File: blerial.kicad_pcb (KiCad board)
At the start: 2 copper layers, 24 x 24 mm, 9 parts, among them J1 Header, SW1 Power Switch, U1 JDY-23-Module, U2 MIC5504-3.3YM5

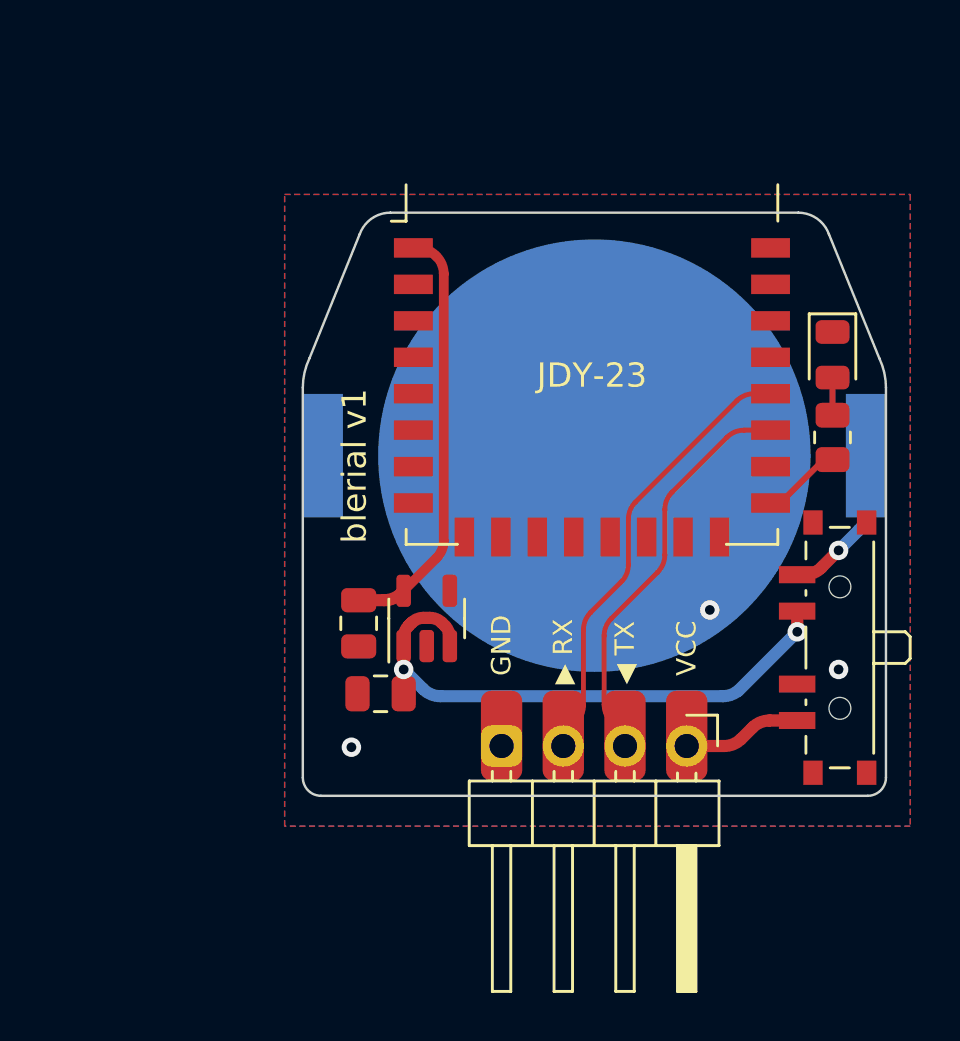
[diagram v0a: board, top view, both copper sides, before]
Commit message: edit to switch between bat / 3.3 regulator
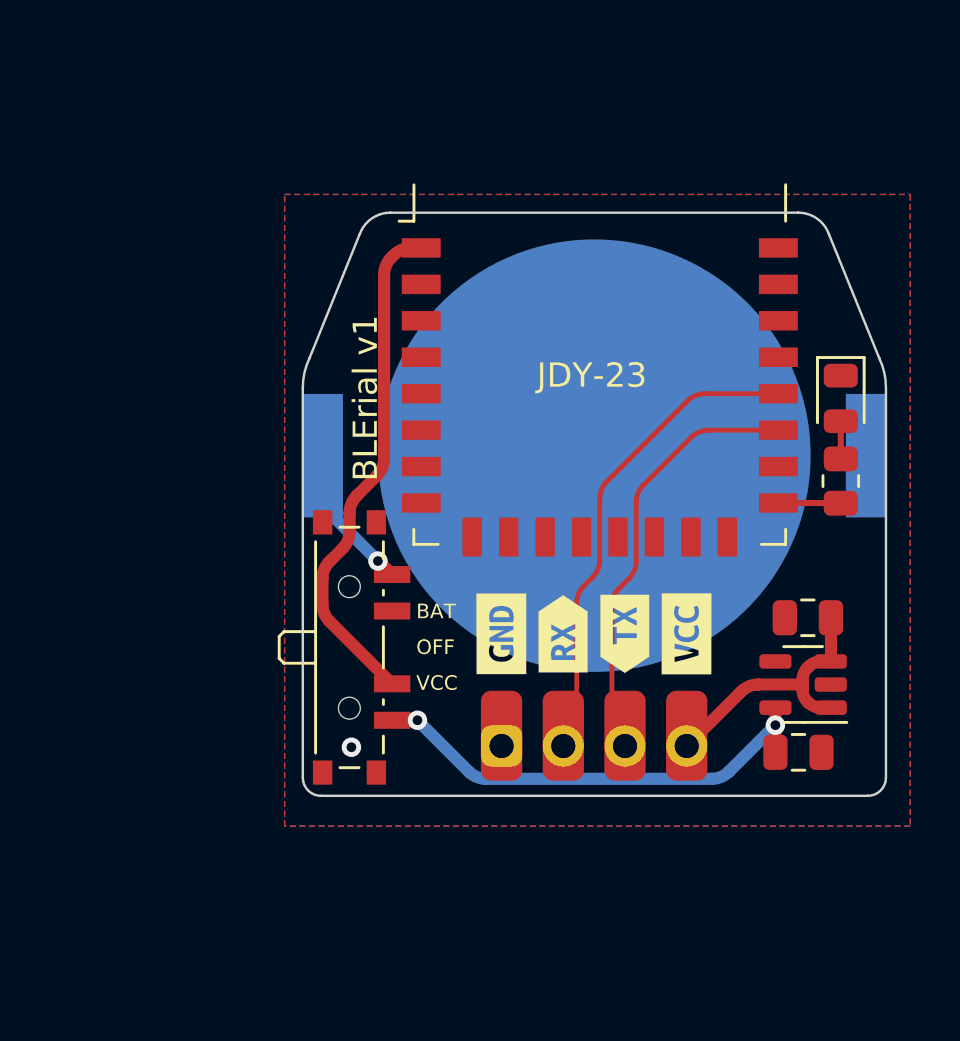
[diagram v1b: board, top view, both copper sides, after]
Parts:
- added kibuzzard-6213ECBD: G***, kibuzzard-6213ECBD, F.Cu at (159.2, 119.3)
- added kibuzzard-6213ECEC: G***, kibuzzard-6213ECEC, F.Cu at (161.7, 119.3)
- added kibuzzard-6213ECF8: G***, kibuzzard-6213ECF8, F.Cu at (164.3, 119.3)
- added kibuzzard-6213ED09: G***, kibuzzard-6213ED09, F.Cu at (166.8, 119.3)
- moved SW1 19.5 mm to (153.2, 119.9), turned to -90 degrees
- moved C2 18.9 mm to (171.4, 124.2), turned to 0 degrees
- moved C1 17.9 mm to (171.8, 118.7)
- moved U2 15.7 mm to (171.6, 121.4), turned to 180 degrees
- moved D1 1.83 mm to (173.1, 109.6)
- moved R1 1.83 mm to (173.1, 113.0)
- moved U1 0.32 mm to (163.2, 108.0)
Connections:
- BT1 pad 1: +BATT -> Net-(BT1-Pad1)
- C1 pad 1: Net-(U2-Pad1) -> VBUS
- J1 pad 1: VCC -> VBUS
- SW1 pad 1: VCC -> Net-(BT1-Pad1)
- SW1 pad 3: Net-(U2-Pad1) -> VCC
- SW1 pad 4: +BATT -> +3V3
- U1 pad 1: +3V3 -> VCC
- U2 pad 1: Net-(U2-Pad1) -> VBUS
- U2 pad 3: Net-(U2-Pad1) -> VBUS
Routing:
- net Net-(U2-Pad1): track 24.0 -> 0.00 mm, vias 2 -> 0
- net VCC: track 4.88 -> 21.0 mm
- net VBUS: track 0.00 -> 11.3 mm
- net +BATT: track 6.39 -> 0.00 mm, vias 1 -> 0
- net Net-(BT1-Pad1): track 0.00 -> 6.05 mm, vias 0 -> 1
- net +3V3: track 17.5 -> 19.4 mm, vias 0 -> 2
- net RXD: track 18.0 -> 19.5 mm
- net TXD: track 16.4 -> 17.3 mm
- net Net-(R1-Pad1): track 3.29 -> 2.56 mm
- net GND: vias 3 -> 1
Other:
- board text added: "2022 ansemjo"
- board text added: "BAT"
- board text added: "BLErial v1"
- board text added: "OFF"
- board text added: "VCC: 3.0-5.5V"
- board text removed: "GND"
- board text removed: "blerial v1"
- board text removed: "▶ RX"
- board text removed: "◀ TX"

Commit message: rerouted for HM-19, but not very tidy
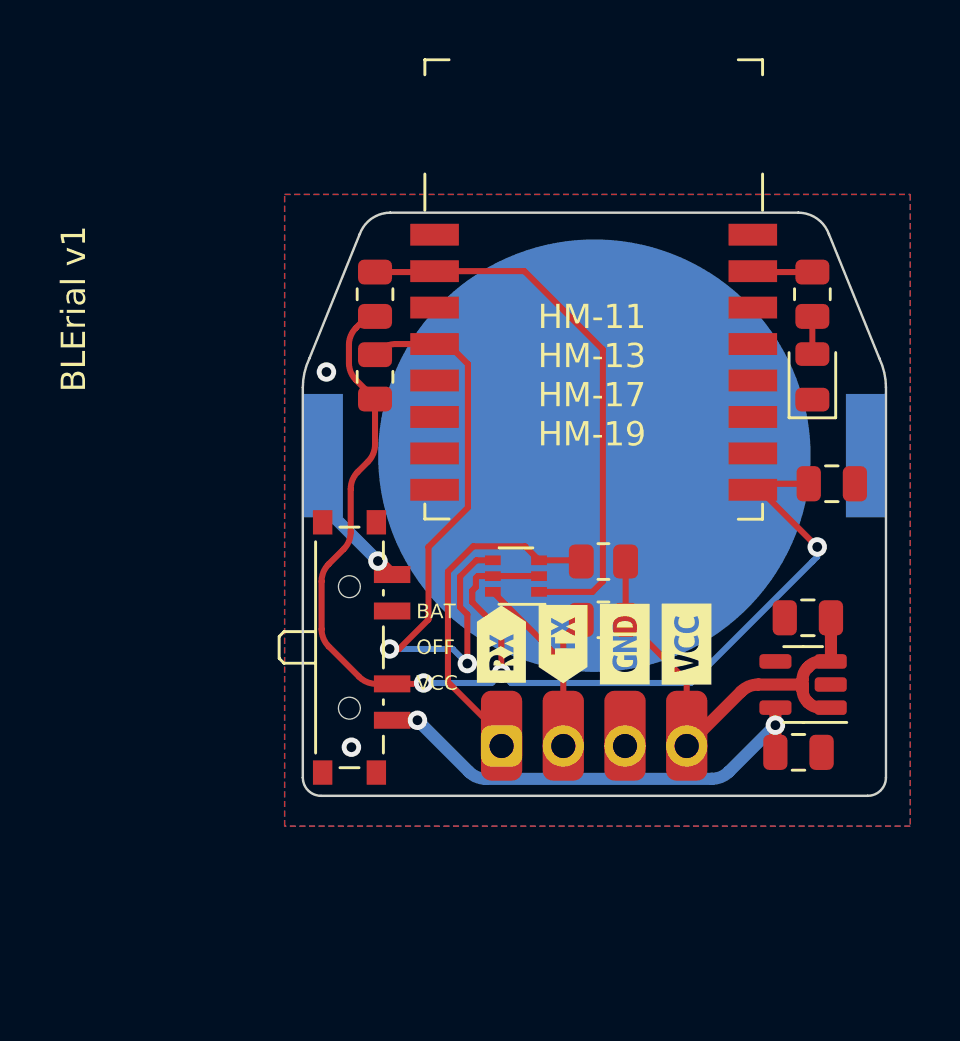
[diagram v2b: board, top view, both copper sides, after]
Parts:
- added C3: 0.1µF, Capacitor_SMD:C_0805_2012Metric, F.Cu at (172.8, 113.2)
- added Q1: BSD840N, Package_TO_SOT_SMD:SOT-363_SC-70-6, F.Cu at (159.8, 117.0)
- added R2: 10kΩ, Resistor_SMD:R_0805_2012Metric, F.Cu at (154.0, 105.4)
- added R3: 10kΩ, Resistor_SMD:R_0805_2012Metric, F.Cu at (163.4, 118.8)
- added R4: 10kΩ, Resistor_SMD:R_0805_2012Metric, F.Cu at (154.0, 108.8)
- added R5: 10kΩ, Resistor_SMD:R_0805_2012Metric, F.Cu at (163.4, 116.4)
- U1: value JDY-23-Module -> HM-19; footprint jdy:JDY-23 -> blerial:HM-19
- moved R1 7.78 mm to (172.0, 105.4)
- moved kibuzzard-6213ECBD 5.10 mm to (164.3, 119.8)
- moved kibuzzard-6213ECF8 2.57 mm to (161.7, 119.8)
- moved kibuzzard-6213ECEC 2.57 mm to (159.2, 119.8)
- moved D1 1.47 mm to (172.0, 108.8), turned to 90 degrees
- moved kibuzzard-6213ED09 0.42 mm to (166.8, 119.8)
- moved U1 0.25 mm to (163.0, 108.1)
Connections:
- J1 pad 2: TXD -> GND
- J1 pad 3: RXD -> TXD_H
- J1 pad 4: GND -> RXD_H
- R1 pad 1: Net-(R1-Pad1) -> Net-(D1-Pad2)
- R1 pad 2: Net-(D1-Pad2) -> Net-(R1-Pad2)
- U1 pad 1: VCC -> unconnected-(U1-Pad1)
- U1 pad 12: unconnected-(U1-Pad12) -> GND
- U1 pad 15: unconnected-(U1-Pad15) -> Net-(R1-Pad2)
- U1 pad 2: unconnected-(U1-Pad2) -> TXD
- U1 pad 4: OUT1 -> RXD
- U1 pad 5: OUT2 -> unconnected-(U1-Pad5)
- U1 pad 6: STAT -> unconnected-(U1-Pad6)
- U1 pad 7: IN7 -> unconnected-(U1-Pad7)
- U1 pad 8: OUT3 -> unconnected-(U1-Pad8)
- U1 pad 9: unconnected-(U1-Pad9) -> VCC
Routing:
- net VCC: track 21.0 -> 52.1 mm, vias 0 -> 3
- net RXD_H: track 0.00 -> 13.8 mm
- net TXD_H: track 0.00 -> 9.60 mm
- net VBUS: track 11.3 -> 19.5 mm
- net RXD: track 19.5 -> 26.4 mm, vias 0 -> 2
- net TXD: track 17.3 -> 23.1 mm
- net Net-(R1-Pad1): track 2.56 -> 0.00 mm
- net Net-(R1-Pad2): track 0.00 -> 2.47 mm
- net GND: vias 1 -> 2
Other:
- board text added: "HM-11 HM-13 HM-17 HM-19"
- board text removed: "JDY-23"

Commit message: finished redesign with 200µm net class, rotated battery
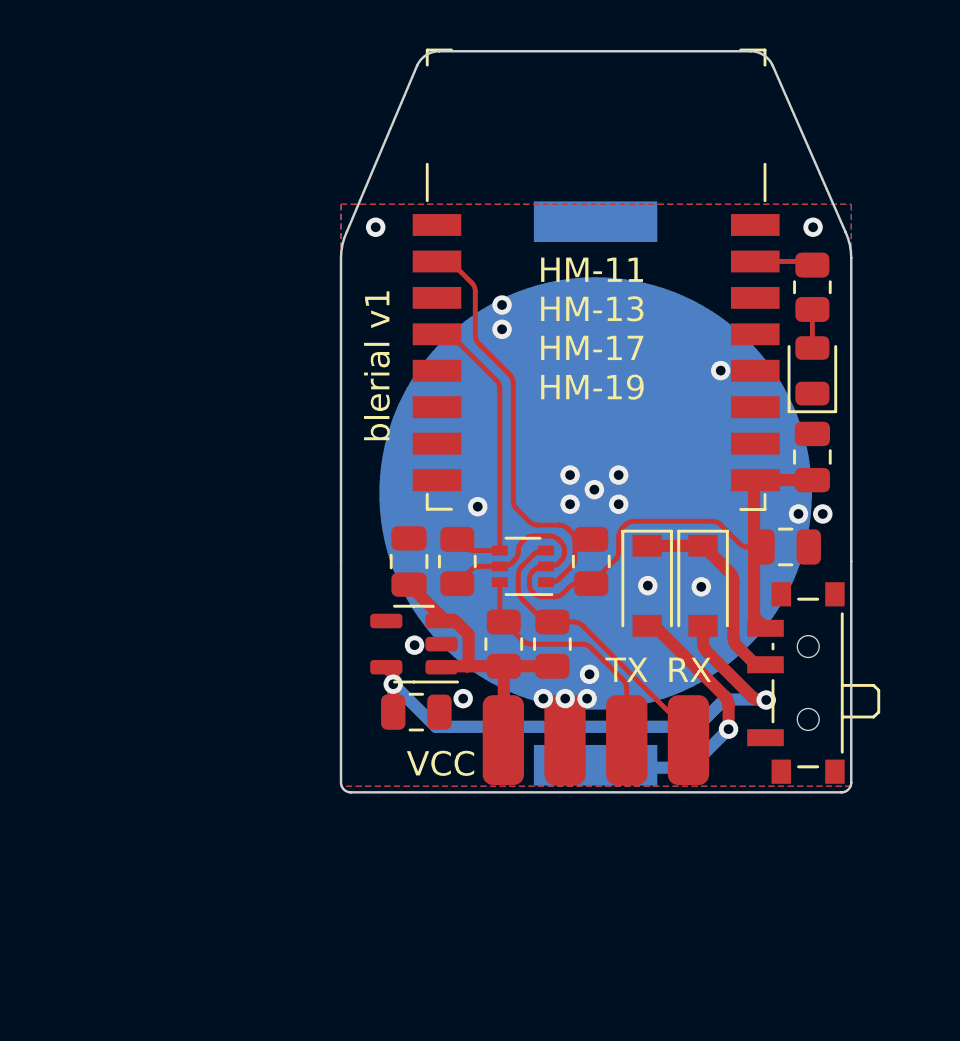
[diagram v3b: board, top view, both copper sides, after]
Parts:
- removed kibuzzard-6213ECBD: G***, kibuzzard-6213ECBD
- removed kibuzzard-6213ECEC: G***, kibuzzard-6213ECEC
- removed kibuzzard-6213ECF8: G***, kibuzzard-6213ECF8
- removed kibuzzard-6213ED09: G***, kibuzzard-6213ED09
- added C4: 1µF, Capacitor_SMD:C_0805_2012Metric, F.Cu at (170.9, 115.8)
- added D2: D_Small, Diode_SMD:D_SOD-123, F.Cu at (167.5, 117.4)
- added D3: D_Small, Diode_SMD:D_SOD-123, F.Cu at (165.2, 117.4)
- added ahoi: 2022, blerial:ahoi, B.Cu at (163.9, 99.1)
- Q1: value BSD840N -> FDG1024NZ
- SW1: value Power Switch -> ON/OFF; footprint Button_Switch_SMD:SW_SP3T_PCM13 -> Button_Switch_SMD:SW_SPDT_PCM12
- moved SW1 18.3 mm to (171.5, 121.4), turned to 90 degrees
- moved C1 16.6 mm to (155.4, 116.4), turned to 90 degrees
- moved U2 16.1 mm to (155.6, 119.8)
- moved C2 15.8 mm to (155.7, 122.6)
- moved R2 14.1 mm to (162.9, 116.4)
- moved R4 8.32 mm to (157.4, 116.4)
- moved R3 4.22 mm to (159.3, 119.8), turned to 90 degrees
- moved R5 4.00 mm to (161.3, 119.8), turned to 90 degrees
- moved BT1 1.56 mm to (163.1, 113.6), turned to -90 degrees
- moved C3 1.36 mm to (172.0, 112.1), turned to 90 degrees
- moved Q1 0.49 mm to (160.1, 116.6)
- moved U1 0.41 mm to (163.1, 107.7)
- moved R1 0.29 mm to (172.0, 105.1)
- moved D1 0.25 mm to (172.0, 108.5)
- moved J1 0.20 mm to (166.9, 124.1)
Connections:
- J1 pad 1: VBUS -> RXD_H
- J1 pad 2: GND -> TXD_H
- J1 pad 3: TXD_H -> GND
- J1 pad 4: RXD_H -> VBUS
- SW1 pad 1: Net-(BT1-Pad1) -> unconnected-(SW1-Pad1)
- SW1 pad 2: unconnected-(SW1-Pad2) -> Net-(SW1-Pad2)
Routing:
- net VCC: track 52.1 -> 28.7 mm, vias 3 -> 0
- net RXD: track 26.4 -> 12.2 mm, vias 2 -> 0
- net Net-(SW1-Pad2): track 0.00 -> 8.43 mm
- net VBUS: track 19.5 -> 12.4 mm
- net TXD: track 23.1 -> 17.1 mm
- net Net-(BT1-Pad1): track 6.05 -> 11.9 mm
- net +3V3: track 19.4 -> 22.9 mm
- net RXD_H: track 13.8 -> 12.0 mm
- net GND: vias 2 -> 21
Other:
- board size 24 x 24 mm -> 21 x 30.5 mm
- board text added: "3.0-5.5V"
- board text added: "RX"
- board text added: "TX"
- board text added: "blerial v1"
- board text removed: "2022 ansemjo"
- board text removed: "BAT"
- board text removed: "BLErial v1"
- board text removed: "OFF"
- board text removed: "VCC: 3.0-5.5V"

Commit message: small tweaks, correct diode and mosfet pns
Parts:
- added kibuzzard-622C9B09: G***, kibuzzard-622C9B09, F.Cu at (154.1, 108.3)
- D2, D3: value D_Small -> 1N5819HW
- Q1: value FDG1024NZ -> BSD840NH6327XTSA1
- moved ahoi 0.15 mm to (163.9, 99.0)
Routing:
- net GND: vias 21 -> 20
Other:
- board text added: "2022 ansemjo"
- board text added: "CR2032"
- board text added: "VCC 3.0-5.5V"
- board text added: "on off"
- board text removed: "blerial v1"
